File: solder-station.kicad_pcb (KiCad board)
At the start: 2 copper layers, 43 parts, among them J1 Temp Sensor, J2 Heating Element, J3 SWD ISP, J4 STM_UART, Q1 BC856BDW1, Q2 NTMFS4937N, Q3 L2N7002M3T5G, Q4 L2N7002M3T5G, U1 LM75B, U2 74LVC1G58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

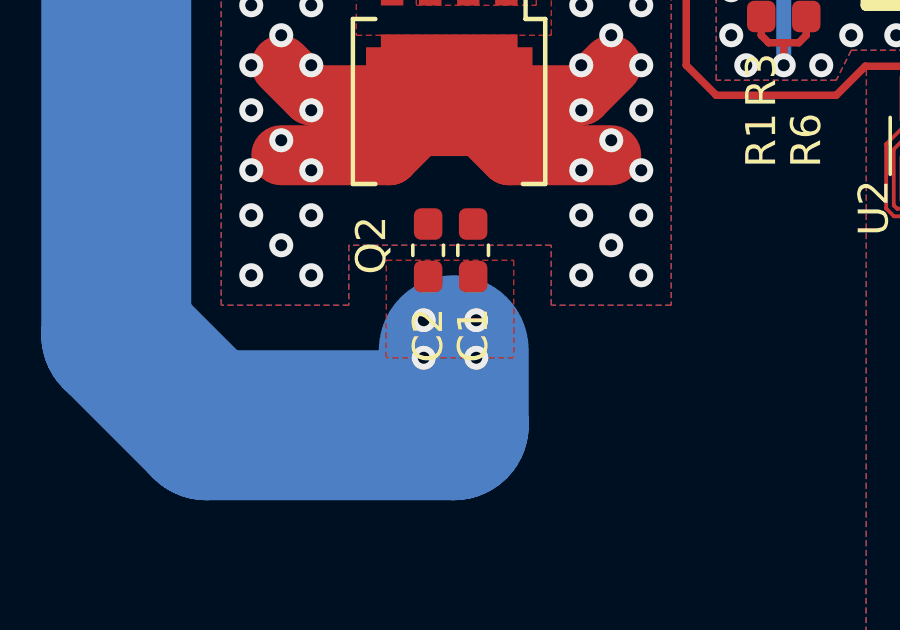
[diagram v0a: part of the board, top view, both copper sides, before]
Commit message: Remove solder mask from mosfet heatsink
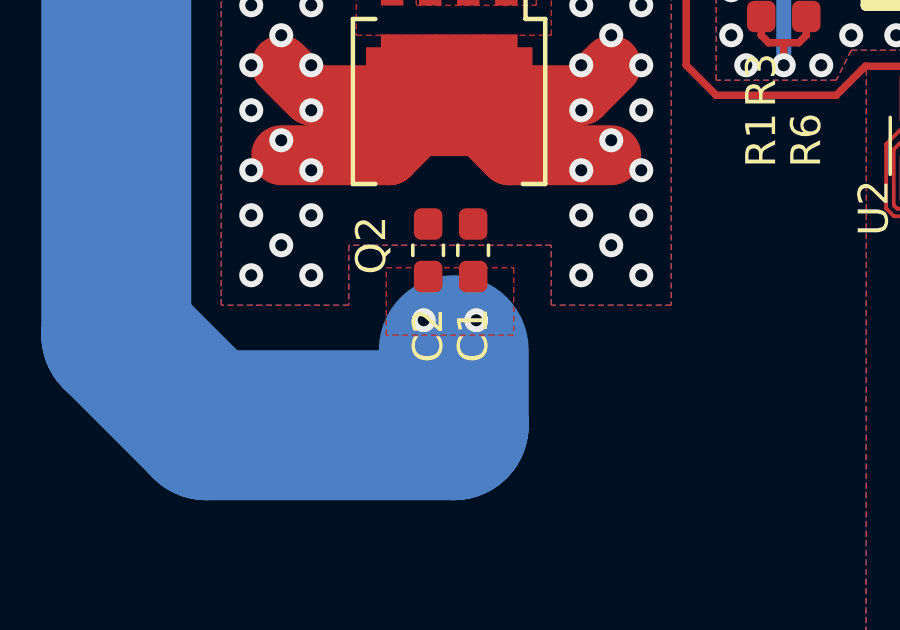
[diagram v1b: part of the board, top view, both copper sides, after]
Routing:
- net GNDPWR: vias 4 -> 2
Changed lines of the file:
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@@
   (general
     (thickness 1.6)
-    (drawings 0)
-    (tracks 465)
+    (drawings 1)
+    (tracks 463)
     (zones 0)
     (modules 43)
@@
     )
   )
-  (via (at 122.5 81.5) (size 0.8) (drill 0.4) (layers F.Cu B.Cu) (net 23))
-  (via (at 126.25 68.75) (size 0.8) (drill 0.4) (layers F.Cu B.Cu) (net 15))
-  (via (at 112 72.25) (size 0.8) (drill 0.4) (layers F.Cu B.Cu) (net 23))
-  (via (at 100.75 71.5) (size 0.8) (drill 0.4) (layers F.Cu B.Cu) (net 23))
-  (via (at 114.25 54.5) (size 0.8) (drill 0.4) (layers F.Cu B.Cu) (net 15))
-  (via (at 125 65.25) (size 0.8) (drill 0.4) (layers F.Cu B.Cu) (net 15))
+  (gr_poly (pts (xy 75.5 78.5) (xy 75.5 67.5) (xy 76.5 63) (xy 80 61.5) (xy 86.5 61.5) (xy 89.5 63) (xy 90.5 67.5) (xy 90.5 78.5) (xy 86.5 78.5) (xy 86.5 76.5) (xy 79.75 76.5) (xy 79.75 78.5)) (layer B.Mask) (width 0.15))
   (segment (start 78.5 71.5) (end 78.5 71.5) (width 2) (layer F.Cu) (net 1))
   (segment (start 83.1 71.5) (end 78.5 71.5) (width 2) (layer F.Cu) (net 1))
@@
   (via (at 82.25 79) (size 0.8) (drill 0.4) (layers F.Cu B.Cu) (net 7))
   (via (at 84 79) (size 0.8) (drill 0.4) (layers F.Cu B.Cu) (net 7))
-  (via (at 82.25 80.25) (size 0.8) (drill 0.4) (layers F.Cu B.Cu) (net 7))
-  (via (at 84 80.25) (size 0.8) (drill 0.4) (layers F.Cu B.Cu) (net 7))
   (segment (start 75 82.5) (end 83.25 82.5) (width 5) (layer B.Cu) (net 7))
   (segment (start 83.25 82.5) (end 83.25 80) (width 5) (layer B.Cu) (net 7))
@@
   (segment (start 124.875 59.375) (end 124.875 61.5) (width 0.25) (layer F.Cu) (net 14))
   (segment (start 124 58.5) (end 124.875 59.375) (width 0.25) (layer F.Cu) (net 14))
+  (via (at 126.25 68.75) (size 0.8) (drill 0.4) (layers F.Cu B.Cu) (net 15))
+  (via (at 114.25 54.5) (size 0.8) (drill 0.4) (layers F.Cu B.Cu) (net 15))
+  (via (at 125 65.25) (size 0.8) (drill 0.4) (layers F.Cu B.Cu) (net 15))
   (segment (start 123.240284 76.953966) (end 121.740284 76.953966) (width 0.25) (layer F.Cu) (net 15))
   (segment (start 117.059556 66.703183) (end 118.559556 66.703183) (width 0.25) (layer F.Cu) (net 15))
@@
   (via (at 123.5 80) (size 0.8) (drill 0.4) (layers F.Cu B.Cu) (net 15))
   (via (at 124.5 80) (size 0.8) (drill 0.4) (layers F.Cu B.Cu) (net 15))
-  (via (at 124.5 78.75) (size 0.8) (drill 0.4) (layers F.Cu B.Cu) (net 17))
-  (via (at 119.75 65) (size 0.8) (drill 0.4) (layers F.Cu B.Cu) (net 17))
-  (via (at 113.25 64.5) (size 0.8) (drill 0.4) (layers F.Cu B.Cu) (net 17))
-  (via (at 94.25 70.5) (size 0.8) (drill 0.4) (layers F.Cu B.Cu) (net 17))
-  (via (at 132 68.25) (size 0.8) (drill 0.4) (layers F.Cu B.Cu) (net 17))
   (segment (start 130.375 63.5) (end 128.625 63.5) (width 0.25) (layer F.Cu) (net 16))
   (segment (start 128.875 61.5) (end 128.875 62.375) (width 0.25) (layer F.Cu) (net 16))
@@
   (segment (start 128.625 64.875) (end 128.625 64.375) (width 0.25) (layer F.Cu) (net 16))
   (segment (start 123.865 69.635) (end 128.625 64.875) (width 0.25) (layer F.Cu) (net 16))
+  (via (at 124.5 78.75) (size 0.8) (drill 0.4) (layers F.Cu B.Cu) (net 17))
+  (via (at 119.75 65) (size 0.8) (drill 0.4) (layers F.Cu B.Cu) (net 17))
+  (via (at 113.25 64.5) (size 0.8) (drill 0.4) (layers F.Cu B.Cu) (net 17))
+  (via (at 94.25 70.5) (size 0.8) (drill 0.4) (layers F.Cu B.Cu) (net 17))
+  (via (at 132 68.25) (size 0.8) (drill 0.4) (layers F.Cu B.Cu) (net 17))
   (segment (start 123.240284 78.703966) (end 121.740284 78.703966) (width 0.25) (layer F.Cu) (net 17))
   (segment (start 121.740284 78.703966) (end 121.115284 78.703966) (width 0.25) (layer F.Cu) (net 17))
@@
   (segment (start 102.458326 70.730566) (end 102.594827 70.594065) (width 0.127) (layer F.Cu) (net 22))
   (segment (start 102.458326 71.607566) (end 102.458326 70.730566) (width 0.127) (layer F.Cu) (net 22))
+  (via (at 122.5 81.5) (size 0.8) (drill 0.4) (layers F.Cu B.Cu) (net 23))
+  (via (at 112 72.25) (size 0.8) (drill 0.4) (layers F.Cu B.Cu) (net 23))
+  (via (at 100.75 71.5) (size 0.8) (drill 0.4) (layers F.Cu B.Cu) (net 23))
   (segment (start 107.740284 76.953966) (end 109.240284 76.953966) (width 0.25) (layer F.Cu) (net 23))
   (segment (start 110.740284 76.953966) (end 111.365284 76.953966) (width 0.25) (layer F.Cu) (net 23))
@@
   (via (at 114.75 80) (size 0.8) (drill 0.4) (layers F.Cu B.Cu) (net 23))
   (via (at 114.75 81) (size 0.8) (drill 0.4) (layers F.Cu B.Cu) (net 23))
-  (via (at 121.25 81.5) (size 0.8) (drill 0.4) (layers F.Cu B.Cu) (net 27))
-  (via (at 106.5 78.75) (size 0.8) (drill 0.4) (layers F.Cu B.Cu) (net 27))
-  (via (at 119 73) (size 0.8) (drill 0.4) (layers F.Cu B.Cu) (net 27))
   (segment (start 99.471825 72.621067) (end 99.608326 72.484566) (width 0.127) (layer F.Cu) (net 24))
   (segment (start 98.594825 72.621067) (end 99.471825 72.621067) (width 0.127) (layer F.Cu) (net 24))
@@
   (segment (start 111.769395 75.535077) (end 97.92371 75.535076) (width 0.127) (layer F.Cu) (net 26))
   (segment (start 113.290284 76.203966) (end 112.438284 76.203966) (width 0.127) (layer F.Cu) (net 26))
+  (via (at 121.25 81.5) (size 0.8) (drill 0.4) (layers F.Cu B.Cu) (net 27))
+  (via (at 106.5 78.75) (size 0.8) (drill 0.4) (layers F.Cu B.Cu) (net 27))
+  (via (at 119 73) (size 0.8) (drill 0.4) (layers F.Cu B.Cu) (net 27))
   (segment (start 107.740284 78.703966) (end 109.240284 78.703966) (width 0.25) (layer F.Cu) (net 27))
   (segment (start 110.740284 78.703966) (end 109.240284 78.703966) (width 0.25) (layer F.Cu) (net 27))
@@
     (polygon
       (pts
-        (xy 81 77) (xy 85.25 77) (xy 85.25 80.25) (xy 81 80.25)
+        (xy 81 77.25) (xy 85.25 77.25) (xy 85.25 79.5) (xy 81 79.5)
       )
     )

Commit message: Fix DRC issues
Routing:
- net Net-(Q1-Pad3): track 8.16 -> 20.9 mm, vias 0 -> 2
- net +3V3: track 60.3 -> 71.3 mm, vias 4 -> 5
- net /IRON_PWR: track 32.2 -> 35.7 mm
- net +3.3VA: track 79.7 -> 76.5 mm
- net /A_THERMO: track 49.6 -> 50.6 mm

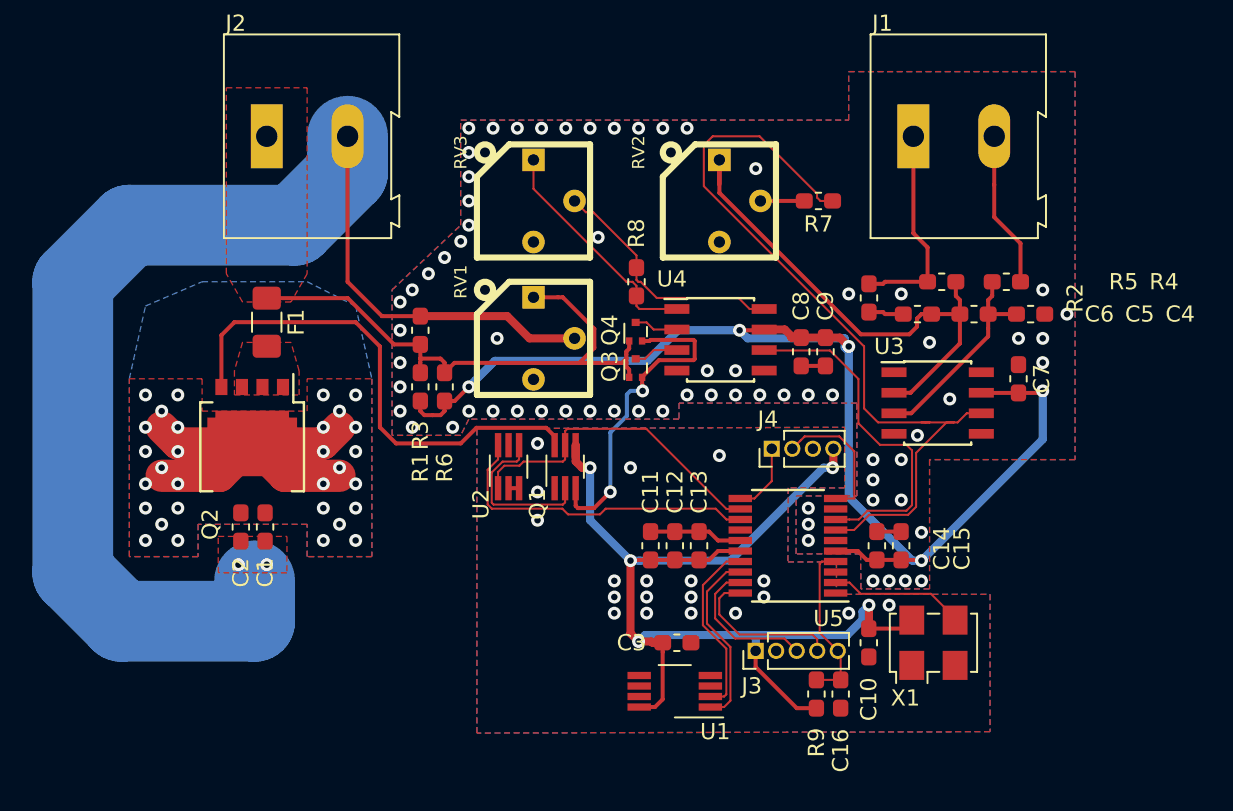
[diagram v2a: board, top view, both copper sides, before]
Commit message: Fix bug where mosfet would not work & reduce cm^2
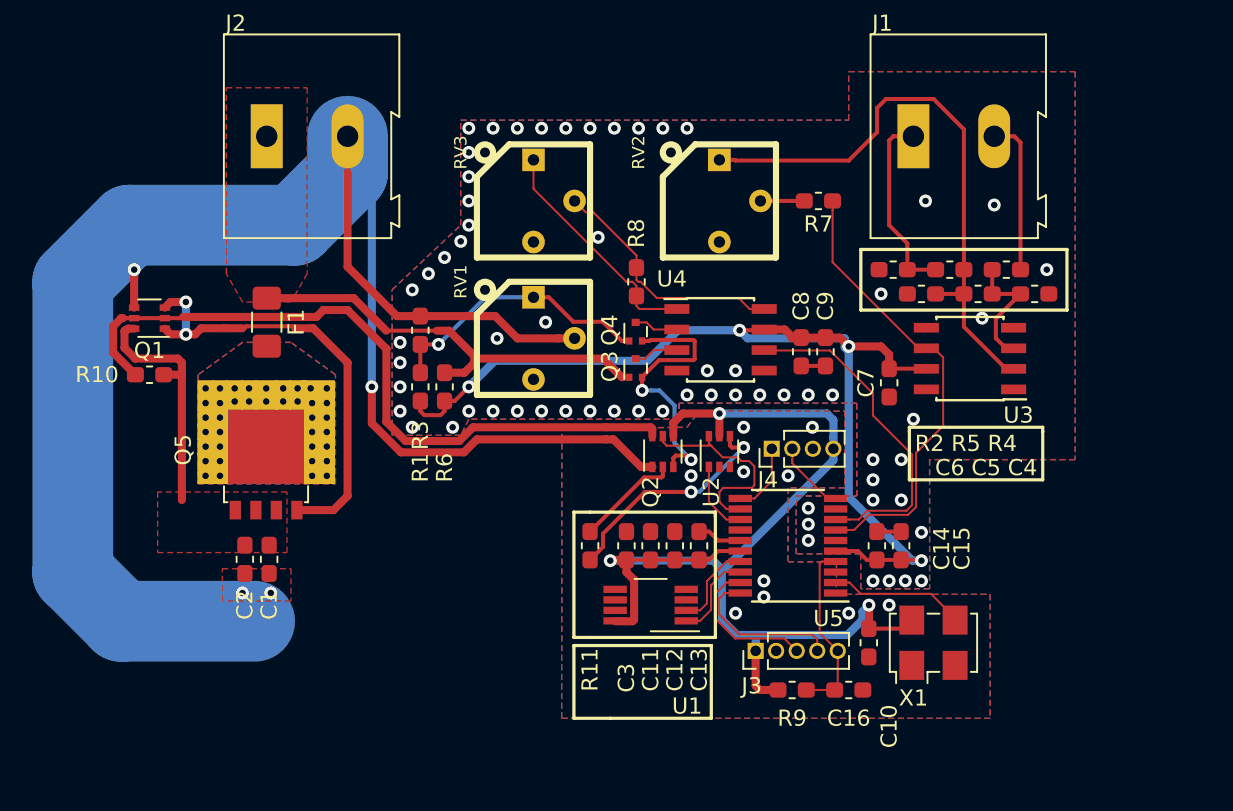
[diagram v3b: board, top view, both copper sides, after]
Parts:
- added Q5: FDMS6681Z, Package_TO_SOT_SMD:LFPAK56_ThermalVias-1, F.Cu at (84.0, 72.8)
- added R10: 10k, Resistor_SMD:R_0603_1608Metric_Pad1.05x0.95mm_HandSolder, F.Cu at (76.8, 67.2)
- added R11: 0, Resistor_SMD:R_0603_1608Metric_Pad1.05x0.95mm_HandSolder, F.Cu at (104.0, 77.8)
- F1: value 20A -> 10A
- Q1: value BC856BDW1 -> MBT3946DW1T1; footprint Package_TO_SOT_SMD:SOT-363_SC-70-6_Handsoldering -> Package_TO_SOT_SMD:SOT-363_SC-70-6
- Q2: value NTMFS4937N -> MBT3946DW1T1; footprint solder-station:ON_S-SO-8_5.3x6.2mm_P1.27mm_TAB488AA -> Package_TO_SOT_SMD:SOT-363_SC-70-6
- U2: value 74LVC1G58 -> 74LVC1G57; footprint Package_TO_SOT_SMD:SOT-363_SC-70-6_Handsoldering -> Package_TO_SOT_SMD:SOT-363_SC-70-6
- moved Q1 27.3 mm to (76.8, 63.8), turned to 180 degrees
- moved Q2 25.4 mm to (108.5, 72.0), turned to 90 degrees
- moved U2 13.1 mm to (112.0, 72.0)
- moved C7 8.00 mm to (122.5, 67.8), turned to 90 degrees
- moved C3 6.76 mm to (106.2, 77.8), turned to 270 degrees
- moved U1 5.53 mm to (107.8, 81.5)
- moved U3 3.40 mm to (127.5, 66.2), turned to 180 degrees
- moved R2 2.30 mm to (122.8, 60.8), turned to 180 degrees
- moved C1 2.02 mm to (84.1, 78.7)
- moved C2 2.02 mm to (82.6, 78.7)
- moved R9 1.52 mm to (116.5, 86.8), turned to 0 degrees
- moved C4 1.27 mm to (131.5, 62.2)
- moved C5 1.27 mm to (128.0, 62.2)
- moved C6 1.27 mm to (124.5, 62.2)
- moved R5 0.90 mm to (126.2, 60.8)
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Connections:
- Q1 pad 1: +10V -> Net-(Q1-Pad1)
- Q1 pad 3: Net-(Q1-Pad3) -> Net-(Q1-Pad1)
- Q1 pad 4: +3V3 -> GNDPWR
- Q1 pad 5: /EN_SEN -> Net-(Q1-Pad2)
- Q1 pad 6: Net-(Q1-Pad6) -> +24V
- Q2 pad 1: Net-(F1-Pad2) -> GNDPWR
- Q2 pad 2: Net-(F1-Pad2) -> Net-(Q2-Pad2)
- Q2 pad 3: Net-(F1-Pad2) -> Net-(Q2-Pad3)
- Q2 pad 4: Net-(Q1-Pad6) -> +3V3
- Q2 pad 5: +24V -> /EN_SEN
- Q3 pad 2: Net-(Q1-Pad3) -> Net-(Q2-Pad3)
- Q4 pad 1: /IRON_PWR -> Net-(Q4-Pad1)
- Q4 pad 2: Net-(Q1-Pad3) -> Net-(Q2-Pad3)
- R1 pad 2: /IRON_PWR -> Net-(Q4-Pad1)
- R3 pad 1: /IRON_PWR -> Net-(Q4-Pad1)
- RV1 pad 1: /IRON_PWR -> Net-(Q4-Pad1)
- U2 pad 1: /EN_SEN -> /EN_PWR
- U2 pad 4: Net-(Q1-Pad2) -> Net-(R11-Pad2)
- U2 pad 5: VCC -> +3V3
- U2 pad 6: /EN_PWR -> /EN_SEN
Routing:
- net GNDPWR: track 79.7 -> 117.5 mm, vias 2 -> 4
- net Net-(Q1-Pad2): track 10.3 -> 44.3 mm
- net Net-(Q1-Pad6): track 31.4 -> 0.00 mm
- net Net-(Q1-Pad1): track 0.00 -> 27.6 mm, vias 0 -> 2
- net /A_THERMO: track 50.6 -> 28.6 mm
- net Net-(Q1-Pad3): track 20.9 -> 0.00 mm, vias 2 -> 0
- net Net-(Q2-Pad3): track 0.00 -> 17.6 mm, vias 0 -> 2
- net Net-(Q4-Pad1): track 0.00 -> 17.0 mm, vias 0 -> 1
- net /EN_PWR: track 20.2 -> 4.56 mm
- net Net-(R11-Pad2): track 0.00 -> 14.5 mm, vias 0 -> 2
- net +3.3VA: track 76.5 -> 64.9 mm, vias 5 -> 4
- net +24V: track 24.5 -> 15.3 mm, vias 30 -> 0
- net /IRON_PWR: track 35.7 -> 27.0 mm
- net /EN_SEN: track 20.2 -> 13.0 mm
- net Net-(Q2-Pad2): track 0.00 -> 6.50 mm
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- added copper zone on B.Cu, net Net-(F1-Pad2)
- removed copper zone on B.Cu, net +24V
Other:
- net class High-current power: clearance 0.4 -> 0.2
